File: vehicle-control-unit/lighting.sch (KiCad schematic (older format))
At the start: 23 parts

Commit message: Finish VCU schematic
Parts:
- R14: renamed from R?; value 100 -> 100E
- gave numbers to parts that had none: 22
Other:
- moved on the sheet: D1, D10, D2, D3, D4, D5, D6, D7, D8, D9, J12, Q1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

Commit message: Review schematics
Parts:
- renumbered D9 to D1, D5 to D10, D10 to D2, D1 to D3, D6 to D4, D2 to D5, D7 to D6, D3 to D7, D4 to D8, D8 to D9, R6 to R10, R7 to R11, R8 to R12, R9 to R13, R10 to R14, R11 to R15, R14 to R6, R15 to R7, R12 to R8, R13 to R9
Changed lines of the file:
@@
 EESchema Schematic File Version 4
-LIBS:vehicle-control-unit-cache
 EELAYER 30 0
 EELAYER END
@@
 $EndComp
 $Comp
-L Device:R R15
+L Device:R R7
 U 1 1 5DE05301
 P 3400 8700
-F 0 "R15" H 3470 8746 50  0000 L CNN
+F 0 "R7" H 3470 8746 50  0000 L CNN
 F 1 "10k" H 3470 8655 50  0000 L CNN
 F 2 "" V 3330 8700 50  0001 C CNN
@@
 $EndComp
 $Comp
-L Device:R R14
+L Device:R R6
 U 1 1 5DE05680
 P 3150 8450
-F 0 "R14" V 2943 8450 50  0000 C CNN
+F 0 "R6" V 2943 8450 50  0000 C CNN
 F 1 "100E" V 3034 8450 50  0000 C CNN
 F 2 "" V 3080 8450 50  0001 C CNN
@@
 $EndComp
 $Comp
-L Device:R R12
+L Device:R R8
 U 1 1 5DE05B60
 P 3600 7900
-F 0 "R12" H 3670 7946 50  0000 L CNN
+F 0 "R8" H 3670 7946 50  0000 L CNN
 F 1 "R" H 3670 7855 50  0000 L CNN
 F 2 "" V 3530 7900 50  0001 C CNN
@@
 $EndComp
 $Comp
-L Device:R R13
+L Device:R R9
 U 1 1 5DE05ED0
 P 4000 7900
-F 0 "R13" H 4070 7946 50  0000 L CNN
+F 0 "R9" H 4070 7946 50  0000 L CNN
 F 1 "R" H 4070 7855 50  0000 L CNN
 F 2 "" V 3930 7900 50  0001 C CNN
@@
 $EndComp
 $Comp
-L Device:LED D9
+L Device:LED D1
 U 1 1 5DE06587
 P 3600 7500
-F 0 "D9" V 3639 7383 50  0000 R CNN
+F 0 "D1" V 3639 7383 50  0000 R CNN
 F 1 "LED" V 3548 7383 50  0000 R CNN
 F 2 "" H 3600 7500 50  0001 C CNN
@@
 $EndComp
 $Comp
-L Device:LED D10
+L Device:LED D2
 U 1 1 5DE06CA4
 P 4000 7500
-F 0 "D10" V 4039 7383 50  0000 R CNN
+F 0 "D2" V 4039 7383 50  0000 R CNN
 F 1 "LED" V 3948 7383 50  0000 R CNN
 F 2 "" H 4000 7500 50  0001 C CNN
@@
 $EndComp
 $Comp
-L Device:LED D6
+L Device:LED D4
 U 1 1 5DE08B62
 P 4700 4600
-F 0 "D6" V 4775 4575 50  0000 R TNN
+F 0 "D4" V 4775 4575 50  0000 R TNN
 F 1 "Red 10mm" H 4700 4700 50  0000 C BNN
 F 2 "" H 4700 4600 50  0001 C CNN
@@
 $EndComp
 $Comp
-L Device:LED D1
+L Device:LED D3
 U 1 1 5DE0A330
 P 4700 4000
-F 0 "D1" V 4775 3975 50  0000 R TNN
+F 0 "D3" V 4775 3975 50  0000 R TNN
 F 1 "Red 10mm" H 4700 4100 50  0000 C BNN
 F 2 "" H 4700 4000 50  0001 C CNN
@@
 $EndComp
 $Comp
-L Device:LED D4
+L Device:LED D8
 U 1 1 5DE0EAFE
 P 6100 4000
-F 0 "D4" V 6175 3975 50  0000 R TNN
+F 0 "D8" V 6175 3975 50  0000 R TNN
 F 1 "Orange 10mm" H 6100 4100 50  0000 C BNN
 F 2 "" H 6100 4000 50  0001 C CNN
@@
 $EndComp
 $Comp
-L Device:R R10
+L Device:R R14
 U 1 1 5DE0EB12
 P 6100 5100
-F 0 "R10" H 6170 5146 50  0000 L CNN
+F 0 "R14" H 6170 5146 50  0000 L CNN
 F 1 "R" H 6170 5055 50  0000 L CNN
 F 2 "" V 6030 5100 50  0001 C CNN
@@
 $EndComp
 $Comp
-L Device:R R11
+L Device:R R15
 U 1 1 5DE0EB26
 P 6500 5100
-F 0 "R11" H 6570 5146 50  0000 L CNN
+F 0 "R15" H 6570 5146 50  0000 L CNN
 F 1 "R" H 6570 5055 50  0000 L CNN
 F 2 "" V 6430 5100 50  0001 C CNN
@@
 $EndComp
 $Comp
-L power:GND #PWR028
+L power:GND #PWR030
 U 1 1 5DE219A4
 P 3800 8950
-F 0 "#PWR028" H 3800 8700 50  0001 C CNN
+F 0 "#PWR030" H 3800 8700 50  0001 C CNN
 F 1 "GND" H 3805 8777 50  0000 C CNN
 F 2 "" H 3800 8950 50  0001 C CNN
@@
 	3000 8450 2600 8450
 $Comp
-L power:+BATT #PWR026
+L power:+BATT #PWR029
 U 1 1 5DE22B0F
 P 3800 7150
-F 0 "#PWR026" H 3800 7000 50  0001 C CNN
+F 0 "#PWR029" H 3800 7000 50  0001 C CNN
 F 1 "+BATT" H 3815 7323 50  0000 C CNN
 F 2 "" H 3800 7150 50  0001 C CNN
@@
 	6300 5350 6500 5350
 $Comp
-L Device:LED D8
+L Device:LED D9
 U 1 1 5DE0EB08
 P 6100 4600
-F 0 "D8" V 6175 4575 50  0000 R TNN
+F 0 "D9" V 6175 4575 50  0000 R TNN
 F 1 "Orange 5mm" H 6100 4700 50  0000 C BNN
 F 2 "" H 6100 4600 50  0001 C CNN
@@
 $EndComp
 $Comp
-L Device:LED D5
+L Device:LED D10
 U 1 1 5DE0EB1C
 P 6500 4000
-F 0 "D5" V 6575 3975 50  0000 R TNN
+F 0 "D10" V 6575 3975 50  0000 R TNN
 F 1 "White 5mm" H 6500 4100 50  0000 C BNN
 F 2 "" H 6500 4000 50  0001 C CNN
@@
 $EndComp
 $Comp
-L power:+BATT #PWR019
+L power:+BATT #PWR032
 U 1 1 5DE93A99
 P 4700 3650
-F 0 "#PWR019" H 4700 3500 50  0001 C CNN
+F 0 "#PWR032" H 4700 3500 50  0001 C CNN
 F 1 "+BATT" H 4715 3823 50  0000 C CNN
 F 2 "" H 4700 3650 50  0001 C CNN
@@
 $EndComp
 $Comp
-L power:+BATT #PWR020
+L power:+BATT #PWR033
 U 1 1 5DE9402F
 P 5500 3650
-F 0 "#PWR020" H 5500 3500 50  0001 C CNN
+F 0 "#PWR033" H 5500 3500 50  0001 C CNN
 F 1 "+BATT" H 5515 3823 50  0000 C CNN
 F 2 "" H 5500 3650 50  0001 C CNN
@@
 $EndComp
 $Comp
-L power:+BATT #PWR021
+L power:+BATT #PWR036
 U 1 1 5DE945F6
 P 6300 3650
-F 0 "#PWR021" H 6300 3500 50  0001 C CNN
+F 0 "#PWR036" H 6300 3500 50  0001 C CNN
 F 1 "+BATT" H 6315 3823 50  0000 C CNN
 F 2 "" H 6300 3650 50  0001 C CNN
@@
 	5600 6650 5600 6750
 $Comp
-L power:+BATT #PWR023
+L power:+BATT #PWR034
 U 1 1 5DEBDC35
 P 5600 6050
-F 0 "#PWR023" H 5600 5900 50  0001 C CNN
+F 0 "#PWR034" H 5600 5900 50  0001 C CNN
 F 1 "+BATT" H 5615 6223 50  0000 C CNN
 F 2 "" H 5600 6050 50  0001 C CNN
@@
 $EndComp
 $Comp
-L power:GND #PWR025
+L power:GND #PWR035
 U 1 1 5DEBE138
 P 5600 6750
-F 0 "#PWR025" H 5600 6500 50  0001 C CNN
+F 0 "#PWR035" H 5600 6500 50  0001 C CNN
 F 1 "GND" H 5605 6577 50  0000 C CNN
 F 2 "" H 5600 6750 50  0001 C CNN
@@
 $EndComp
 $Comp
-L power:GND #PWR024
+L power:GND #PWR028
 U 1 1 5DEC191A
 P 3600 6350
-F 0 "#PWR024" H 3600 6100 50  0001 C CNN
+F 0 "#PWR028" H 3600 6100 50  0001 C CNN
 F 1 "GND" H 3605 6177 50  0000 C CNN
 F 2 "" H 3600 6350 50  0001 C CNN
@@
 	5700 4950 5700 4150
 $Comp
-L Device:R R9
+L Device:R R13
 U 1 1 5DE0CEAF
 P 5700 5100
-F 0 "R9" H 5770 5146 50  0000 L CNN
+F 0 "R13" H 5770 5146 50  0000 L CNN
 F 1 "R" H 5770 5055 50  0000 L CNN
 F 2 "" V 5630 5100 50  0001 C CNN
@@
 $EndComp
 $Comp
-L Device:LED D3
+L Device:LED D7
 U 1 1 5DE0C5C7
 P 5700 4000
-F 0 "D3" V 5775 3975 50  0000 R TNN
+F 0 "D7" V 5775 3975 50  0000 R TNN
 F 1 "White 5mm" H 5700 4100 50  0000 C BNN
 F 2 "" H 5700 4000 50  0001 C CNN
@@
 	5500 3750 5300 3750
 $Comp
-L Device:R R8
+L Device:R R12
 U 1 1 5DE0C01C
 P 5300 5100
-F 0 "R8" H 5370 5146 50  0000 L CNN
+F 0 "R12" H 5370 5146 50  0000 L CNN
 F 1 "R" H 5370 5055 50  0000 L CNN
 F 2 "" V 5230 5100 50  0001 C CNN
@@
 	5300 4450 5300 4150
 $Comp
-L Device:LED D7
+L Device:LED D6
 U 1 1 5DE0B3F5
 P 5300 4600
-F 0 "D7" V 5375 4575 50  0000 R TNN
+F 0 "D6" V 5375 4575 50  0000 R TNN
 F 1 "Orange 5mm" H 5300 4700 50  0000 C BNN
 F 2 "" H 5300 4600 50  0001 C CNN
@@
 $EndComp
 $Comp
-L Device:LED D2
+L Device:LED D5
 U 1 1 5DE0AB28
 P 5300 4000
-F 0 "D2" V 5375 3975 50  0000 R TNN
+F 0 "D5" V 5375 3975 50  0000 R TNN
 F 1 "Orange 10mm" H 5300 4100 50  0000 C BNN
 F 2 "" H 5300 4000 50  0001 C CNN
@@
 	4900 4850 4900 4950
 $Comp
-L Device:R R7
+L Device:R R11
 U 1 1 5DE09B97
 P 4900 5100
-F 0 "R7" H 4970 5146 50  0000 L CNN
+F 0 "R11" H 4970 5146 50  0000 L CNN
 F 1 "R" H 4970 5055 50  0000 L CNN
 F 2 "" V 4830 5100 50  0001 C CNN
@@
 	4500 4950 4500 4850
 $Comp
-L Device:R R6
+L Device:R R10
 U 1 1 5DE096EB
 P 4500 5100
-F 0 "R6" H 4570 5146 50  0000 L CNN
+F 0 "R10" H 4570 5146 50  0000 L CNN
 F 1 "R" H 4570 5055 50  0000 L CNN
 F 2 "" V 4430 5100 50  0001 C CNN
@@
 $EndComp
 $Comp
-L power:+BATT #PWR022
+L power:+BATT #PWR031
 U 1 1 5DE4AC10
 P 4100 5050
-F 0 "#PWR022" H 4100 4900 50  0001 C CNN
+F 0 "#PWR031" H 4100 4900 50  0001 C CNN
 F 1 "+BATT" H 4115 5223 50  0000 C CNN
 F 2 "" H 4100 5050 50  0001 C CNN

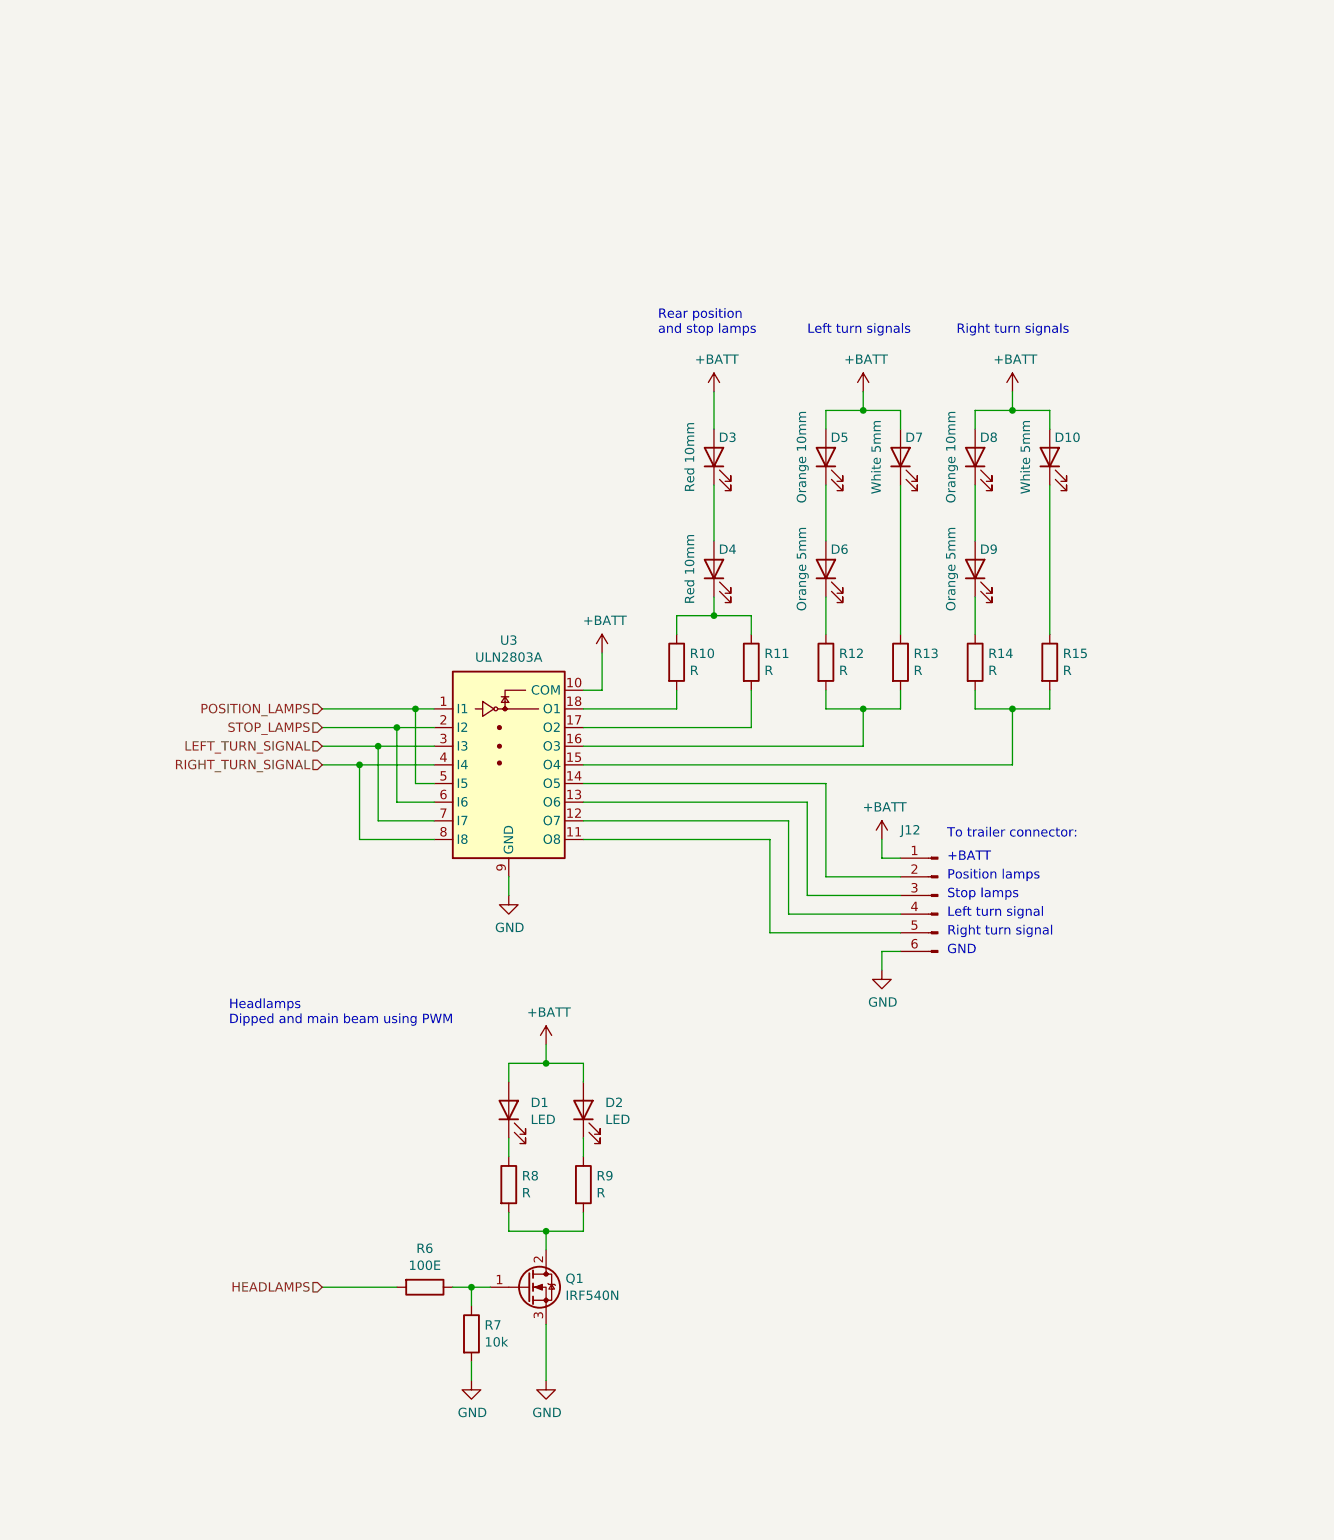
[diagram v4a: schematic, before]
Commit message: Fix some errors in the VCU hardware
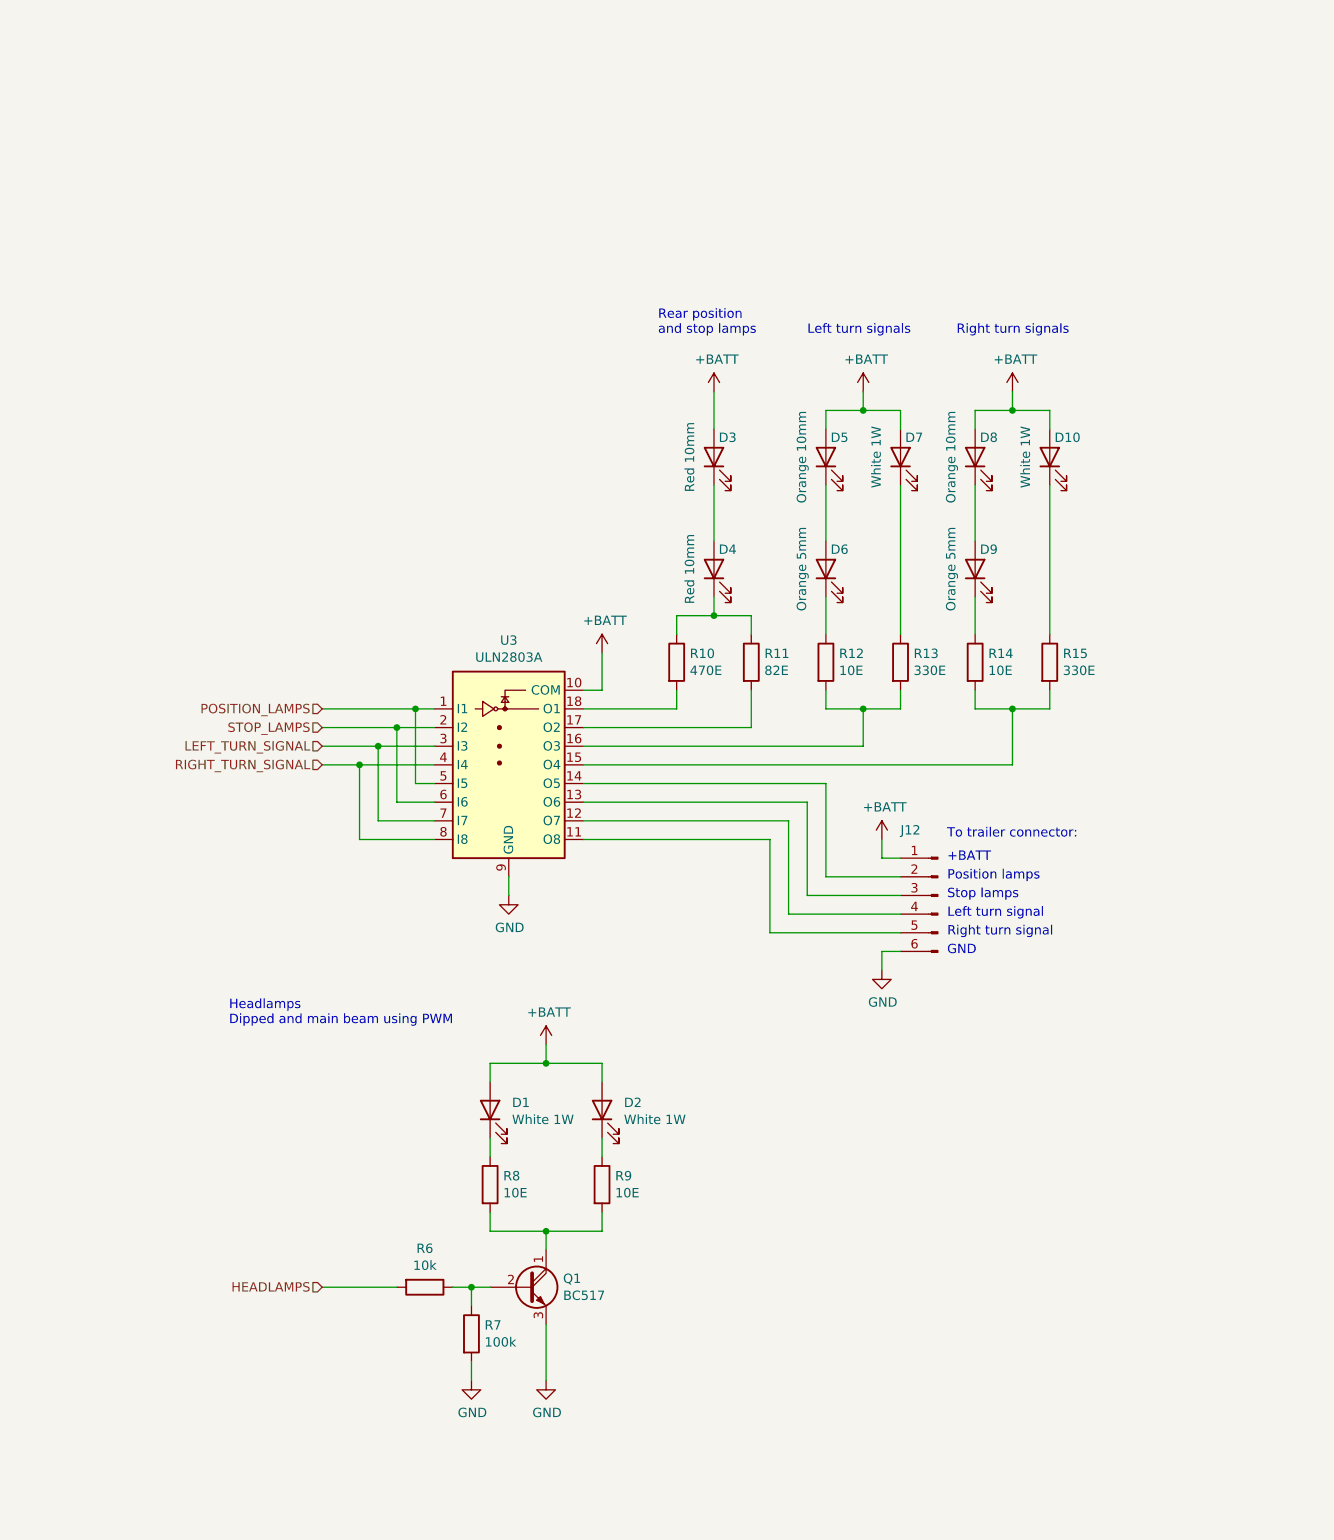
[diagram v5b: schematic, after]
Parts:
- removed Q1: IRF540N, Package_TO_SOT_THT:TO-220-3_Vertical, symbol Transistor_FET:IRF540N
- added Q1: BC517, Package_TO_SOT_THT:TO-92_Inline, symbol Transistor_BJT:BC517
- D1, D2: value LED -> White 1W
- D10, D7: value White 5mm -> White 1W
- R10: value R -> 470E
- R11: value R -> 82E
- R12, R14, R8, R9: value R -> 10E
- R13, R15: value R -> 330E
- R6: value 100E -> 10k
- R7: value 10k -> 100k
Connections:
- net GND: now also Q1.3 (E)
- net at R6.1, R7.1: now also Q1.2 (B)
- net at R8.2, R9.2: now also Q1.1 (C)
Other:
- moved on the sheet: D1, D2, R8, R9
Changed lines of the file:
@@
 Sheet 2 3
 Title "Earth Rover"
-Date "2019-12-21"
-Rev "4"
+Date "2020-02-23"
+Rev "5"
 Comp "Vijfendertig BVBA"
 Comment1 "Maarten De Munck"
@@
 $EndComp
 $Comp
-L Transistor_FET:IRF540N Q1
-U 1 1 5DE047D6
-P 3700 8450
-F 0 "Q1" H 3904 8496 50  0000 L CNN
-F 1 "IRF540N" H 3904 8405 50  0000 L CNN
-F 2 "Package_TO_SOT_THT:TO-220-3_Vertical" H 3950 8375 50  0001 L CIN
-F 3 "http://www.irf.com/product-info/datasheets/data/irf540n.pdf" H 3700 8450 50  0001 L CNN
-	1    3700 8450
-	1    0    0    -1
-$EndComp
-$Comp
 L Device:R R7
 U 1 1 5DE05301
 P 3400 8700
 F 0 "R7" H 3470 8746 50  0000 L CNN
-F 1 "10k" H 3470 8655 50  0000 L CNN
+F 1 "100k" H 3470 8655 50  0000 L CNN
 F 2 "" V 3330 8700 50  0001 C CNN
 F 3 "~" H 3400 8700 50  0001 C CNN
@@
 P 3150 8450
 F 0 "R6" V 2943 8450 50  0000 C CNN
-F 1 "100E" V 3034 8450 50  0000 C CNN
+F 1 "10k" V 3034 8450 50  0000 C CNN
 F 2 "" V 3080 8450 50  0001 C CNN
 F 3 "~" H 3150 8450 50  0001 C CNN
@@
 L Device:R R8
 U 1 1 5DE05B60
-P 3600 7900
-F 0 "R8" H 3670 7946 50  0000 L CNN
-F 1 "R" H 3670 7855 50  0000 L CNN
-F 2 "" V 3530 7900 50  0001 C CNN
-F 3 "~" H 3600 7900 50  0001 C CNN
-	1    3600 7900
+P 3500 7900
+F 0 "R8" H 3570 7946 50  0000 L CNN
+F 1 "10E" H 3570 7855 50  0000 L CNN
+F 2 "" V 3430 7900 50  0001 C CNN
+F 3 "~" H 3500 7900 50  0001 C CNN
+	1    3500 7900
 	1    0    0    -1
 $EndComp
@@
 L Device:R R9
 U 1 1 5DE05ED0
-P 4000 7900
-F 0 "R9" H 4070 7946 50  0000 L CNN
-F 1 "R" H 4070 7855 50  0000 L CNN
-F 2 "" V 3930 7900 50  0001 C CNN
-F 3 "~" H 4000 7900 50  0001 C CNN
-	1    4000 7900
+P 4100 7900
+F 0 "R9" H 4170 7946 50  0000 L CNN
+F 1 "10E" H 4170 7855 50  0000 L CNN
+F 2 "" V 4030 7900 50  0001 C CNN
+F 3 "~" H 4100 7900 50  0001 C CNN
+	1    4100 7900
 	1    0    0    -1
 $EndComp
@@
 L Device:LED D1
 U 1 1 5DE06587
-P 3600 7500
-F 0 "D1" V 3639 7383 50  0000 R CNN
-F 1 "LED" V 3548 7383 50  0000 R CNN
-F 2 "" H 3600 7500 50  0001 C CNN
-F 3 "~" H 3600 7500 50  0001 C CNN
-	1    3600 7500
+P 3500 7500
+F 0 "D1" V 3539 7383 50  0000 R CNN
+F 1 "White 1W" V 3448 7383 50  0000 R CNN
+F 2 "" H 3500 7500 50  0001 C CNN
+F 3 "~" H 3500 7500 50  0001 C CNN
+	1    3500 7500
 	0    -1   -1   0
 $EndComp
@@
 L Device:LED D2
 U 1 1 5DE06CA4
-P 4000 7500
-F 0 "D2" V 4039 7383 50  0000 R CNN
-F 1 "LED" V 3948 7383 50  0000 R CNN
-F 2 "" H 4000 7500 50  0001 C CNN
-F 3 "~" H 4000 7500 50  0001 C CNN
-	1    4000 7500
+P 4100 7500
+F 0 "D2" V 4139 7383 50  0000 R CNN
+F 1 "White 1W" V 4048 7383 50  0000 R CNN
+F 2 "" H 4100 7500 50  0001 C CNN
+F 3 "~" H 4100 7500 50  0001 C CNN
+	1    4100 7500
 	0    -1   -1   0
 $EndComp
@@
 P 6100 5100
 F 0 "R14" H 6170 5146 50  0000 L CNN
-F 1 "R" H 6170 5055 50  0000 L CNN
+F 1 "10E" H 6170 5055 50  0000 L CNN
 F 2 "" V 6030 5100 50  0001 C CNN
 F 3 "~" H 6100 5100 50  0001 C CNN
@@
 P 6500 5100
 F 0 "R15" H 6570 5146 50  0000 L CNN
-F 1 "R" H 6570 5055 50  0000 L CNN
+F 1 "330E" H 6570 5055 50  0000 L CNN
 F 2 "" V 6430 5100 50  0001 C CNN
 F 3 "~" H 6500 5100 50  0001 C CNN
@@
 $EndComp
 Wire Wire Line
-	3600 7650 3600 7750
-Wire Wire Line
-	4000 7650 4000 7750
-Wire Wire Line
-	4000 8050 4000 8150
-Wire Wire Line
-	4000 8150 3800 8150
-Wire Wire Line
-	3600 8150 3600 8050
+	3500 7650 3500 7750
+Wire Wire Line
+	4100 7650 4100 7750
+Wire Wire Line
+	4100 8050 4100 8150
+Wire Wire Line
+	4100 8150 3800 8150
+Wire Wire Line
+	3500 8150 3500 8050
 Wire Wire Line
 	3800 8150 3800 8250
 Connection ~ 3800 8150
 Wire Wire Line
-	3800 8150 3600 8150
+	3800 8150 3500 8150
 Wire Wire Line
 	3500 8450 3400 8450
@@
 	3800 7150 3800 7250
 Wire Wire Line
-	3800 7250 4000 7250
-Wire Wire Line
-	4000 7250 4000 7350
-Wire Wire Line
-	3800 7250 3600 7250
-Wire Wire Line
-	3600 7250 3600 7350
+	3800 7250 4100 7250
+Wire Wire Line
+	4100 7250 4100 7350
+Wire Wire Line
+	3800 7250 3500 7250
+Wire Wire Line
+	3500 7250 3500 7350
 Connection ~ 3800 7250
 Wire Wire Line
@@
 P 6500 4000
 F 0 "D10" V 6575 3975 50  0000 R TNN
-F 1 "White 5mm" H 6500 4100 50  0000 C BNN
+F 1 "White 1W" H 6500 4100 50  0000 C BNN
 F 2 "" H 6500 4000 50  0001 C CNN
 F 3 "~" H 6500 4000 50  0001 C CNN
@@
 P 5700 5100
 F 0 "R13" H 5770 5146 50  0000 L CNN
-F 1 "R" H 5770 5055 50  0000 L CNN
+F 1 "330E" H 5770 5055 50  0000 L CNN
 F 2 "" V 5630 5100 50  0001 C CNN
 F 3 "~" H 5700 5100 50  0001 C CNN
@@
 P 5700 4000
 F 0 "D7" V 5775 3975 50  0000 R TNN
-F 1 "White 5mm" H 5700 4100 50  0000 C BNN
+F 1 "White 1W" H 5700 4100 50  0000 C BNN
 F 2 "" H 5700 4000 50  0001 C CNN
 F 3 "~" H 5700 4000 50  0001 C CNN
@@
 P 5300 5100
 F 0 "R12" H 5370 5146 50  0000 L CNN
-F 1 "R" H 5370 5055 50  0000 L CNN
+F 1 "10E" H 5370 5055 50  0000 L CNN
 F 2 "" V 5230 5100 50  0001 C CNN
 F 3 "~" H 5300 5100 50  0001 C CNN
@@
 P 4900 5100
 F 0 "R11" H 4970 5146 50  0000 L CNN
-F 1 "R" H 4970 5055 50  0000 L CNN
+F 1 "82E" H 4970 5055 50  0000 L CNN
 F 2 "" V 4830 5100 50  0001 C CNN
 F 3 "~" H 4900 5100 50  0001 C CNN
@@
 P 4500 5100
 F 0 "R10" H 4570 5146 50  0000 L CNN
-F 1 "R" H 4570 5055 50  0000 L CNN
+F 1 "470E" H 4570 5055 50  0000 L CNN
 F 2 "" V 4430 5100 50  0001 C CNN
 F 3 "~" H 4500 5100 50  0001 C CNN
@@
 Wire Wire Line
 	5000 6550 5700 6550
+$Comp
+L Transistor_BJT:BC517 Q1
+U 1 1 5E5387A1
+P 3700 8450
+F 0 "Q1" H 3891 8496 50  0000 L CNN
+F 1 "BC517" H 3891 8405 50  0000 L CNN
+F 2 "Package_TO_SOT_THT:TO-92_Inline" H 3900 8375 50  0001 L CIN
+F 3 "http://www.fairchildsemi.com/ds/BC/BC517.pdf" H 3700 8450 50  0001 L CNN
+	1    3700 8450
+	1    0    0    -1
+$EndComp
 $EndSCHEMATC
